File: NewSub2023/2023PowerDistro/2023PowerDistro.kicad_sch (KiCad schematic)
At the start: 17 parts, among them J1 Battery 1 Input, J2 Battery 2 Input, Q1 NMOS, Q2 NMOS, SW1 Power Switch, U1 L7805

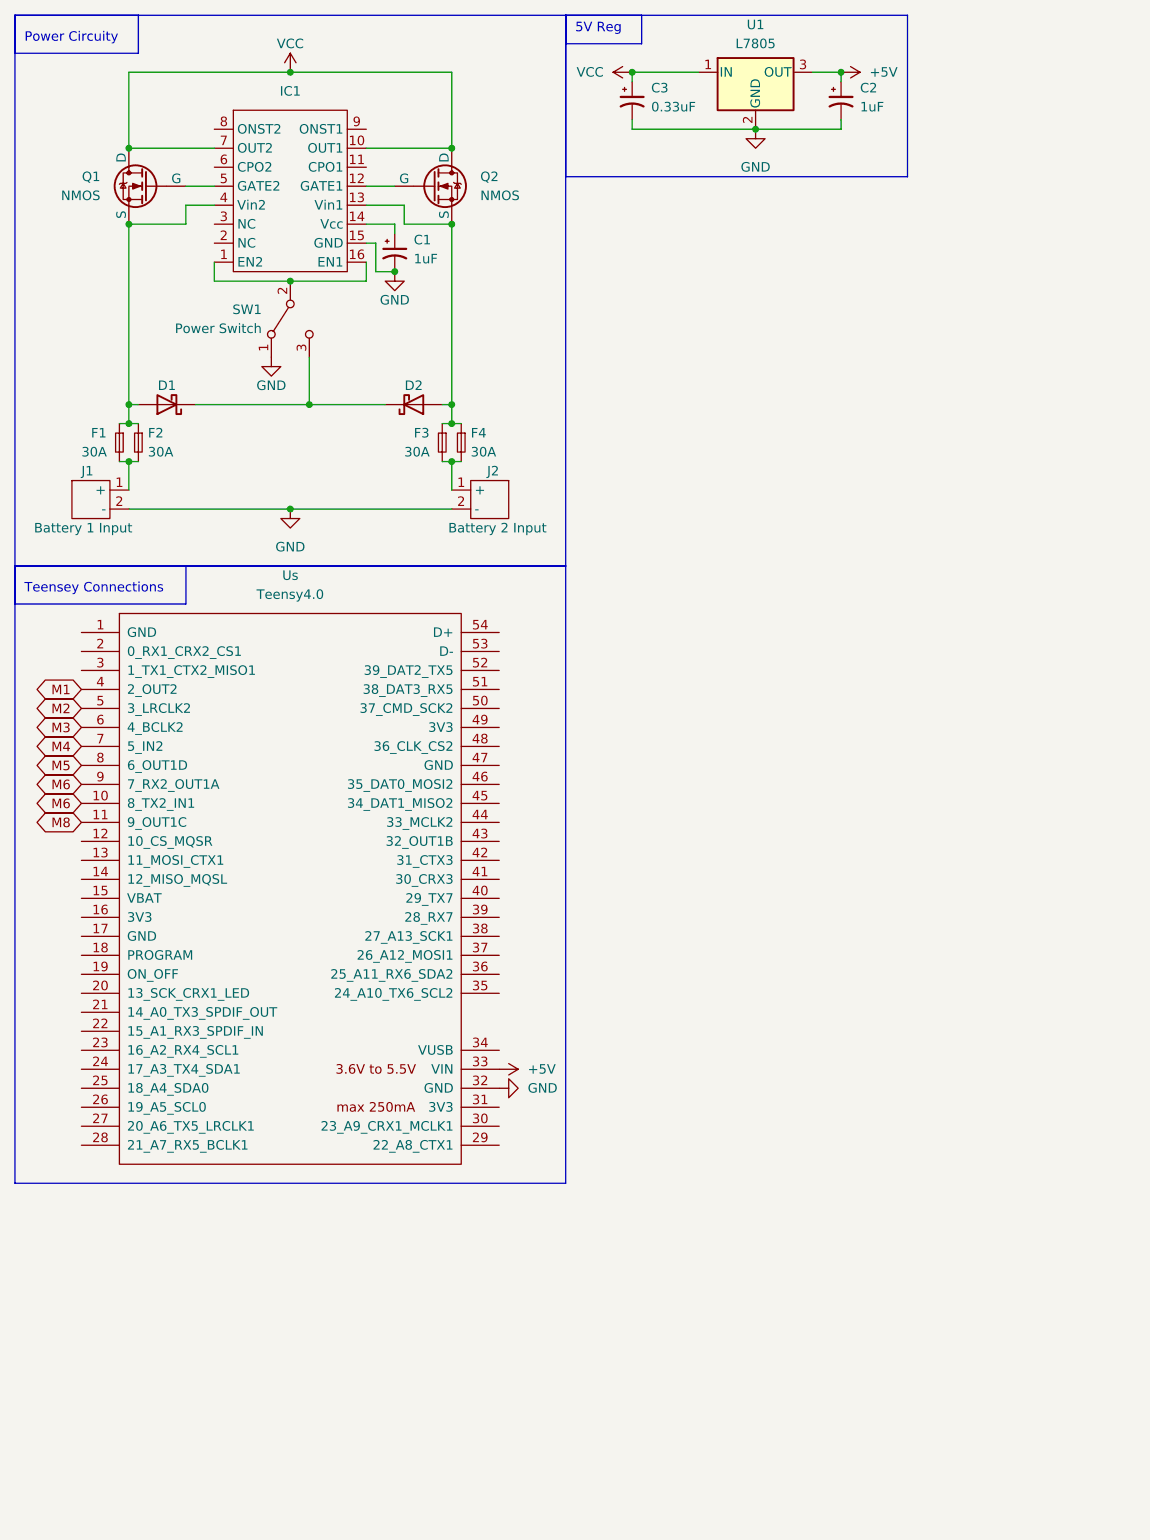
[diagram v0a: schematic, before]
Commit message: Matched footprints to schematic. laid out basic pcb design.
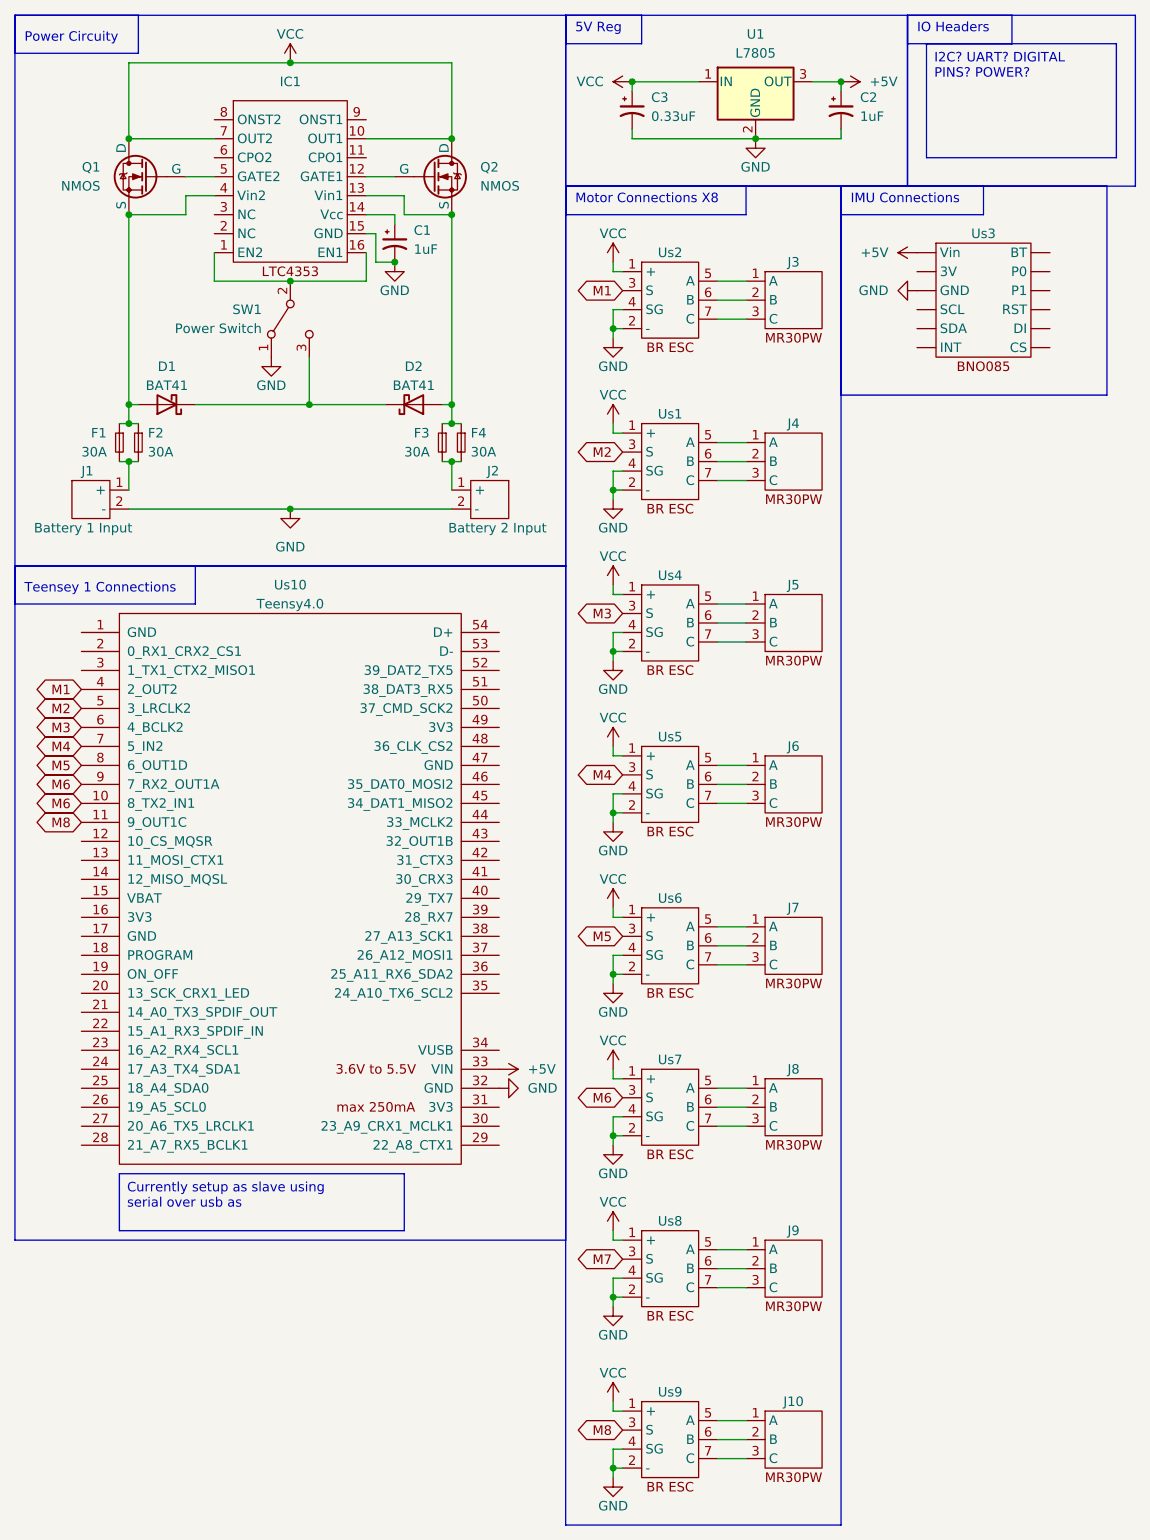
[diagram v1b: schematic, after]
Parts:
- added J10, J3, J4, J5, J6, J7, J8, J9: ~, 2023Footprints:MR30PW-M, symbol 2023Symbols:MR30PW-M
- added Us1, Us2, Us4, Us5, Us6, Us7, Us8, Us9: ~, 2023Footprints:BR-ESC, symbol 2023Symbols:BR-ESC
- added Us3: ~, 2023Footprints:BR-ESC, symbol 2023Symbols:BNO085
- C1, C2, C3: footprint (none) -> Capacitor_THT:CP_Radial_D5.0mm_P2.00mm
- D1, D2: value ~ -> BAT41; footprint (none) -> Diode_THT:D_DO-35_SOD27_P7.62mm_Horizontal
- F1, F2, F3, F4: footprint (none) -> 2023Footprints:3557-15
- IC1: footprint (none) -> Package_SO:MSOP-16_3x4mm_P0.5mm
- J1, J2: footprint (none) -> 2023Footprints:XT90PW-M
- SW1: footprint (none) -> 2023Footprints:MR30PW-M
- renumbered Us to Us10
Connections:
- net +5V: now also Us3. (Vin)
- net GND: now also Us1.2 (-), Us1.4 (SG), Us2.2 (-), Us2.4 (SG), Us3. (Vin), Us4.2 (-), Us4.4 (SG), Us5.2 (-), Us5.4 (SG), Us6.2 (-), Us6.4 (SG), Us7.2 (-), Us7.4 (SG), Us8.2 (-), Us8.4 (SG), Us9.2 (-), Us9.4 (SG)
- net M1: now also Us2.3 (S)
- net M2: now also Us1.3 (S)
- net M3: now also Us4.3 (S)
- net M4: now also Us5.3 (S)
- net M5: now also Us6.3 (S)
- net M6: now also Us7.3 (S)
- net M8: now also Us9.3 (S)
- net VCC: now also Us1.1 (+), Us2.1 (+), Us4.1 (+), Us5.1 (+), Us6.1 (+), Us7.1 (+), Us8.1 (+), Us9.1 (+)
- new net: J4.1 (A), Us1.5 (A)
- new net: J4.2 (B), Us1.6 (B)
- new net: J4.3 (C), Us1.7 (C)
- new net: J9.1 (A), Us8.5 (A)
- new net: J9.2 (B), Us8.6 (B)
- new net: J9.3 (C), Us8.7 (C)
- new net: J7.1 (A), Us6.5 (A)
- new net: J7.2 (B), Us6.6 (B)
- new net: J7.3 (C), Us6.7 (C)
- new net: J10.1 (A), Us9.5 (A)
- new net: J10.2 (B), Us9.6 (B)
- new net: J10.3 (C), Us9.7 (C)
- new net: J6.1 (A), Us5.5 (A)
- new net: J6.2 (B), Us5.6 (B)
- new net: J6.3 (C), Us5.7 (C)
- new net: J5.1 (A), Us4.5 (A)
- new net: J5.2 (B), Us4.6 (B)
- new net: J5.3 (C), Us4.7 (C)
- new net: J8.1 (A), Us7.5 (A)
- new net: J8.2 (B), Us7.6 (B)
- new net: J8.3 (C), Us7.7 (C)
- new net: J3.1 (A), Us2.5 (A)
- new net: J3.2 (B), Us2.6 (B)
- new net: J3.3 (C), Us2.7 (C)
- new net M7: Us8.3 (S)
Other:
- note added: "IMU Connections"
- note added: "IO Headers"
- note added: "Motor Connections X8"
- note added: "Teensey 1 Connections"
- note removed: "Teensey Connections"
- moved on the sheet: C1, C2, C3, Q1, Q2, U1
